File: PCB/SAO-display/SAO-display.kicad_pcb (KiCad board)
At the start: 2 copper layers, 69.3 x 80 mm, 48 parts, among them CON1 SAO v1.69bis badge, J1 Conn_01x02, J2 Conn_01x02, J3 Conn_01x02, J4 Conn_01x02, J5 Conn_01x02, J6 Conn_01x02, M1 AliExpress 3256801443409123 M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, M1 AliExpress 3256806041034057, M1 AliExpress 3256806122258440

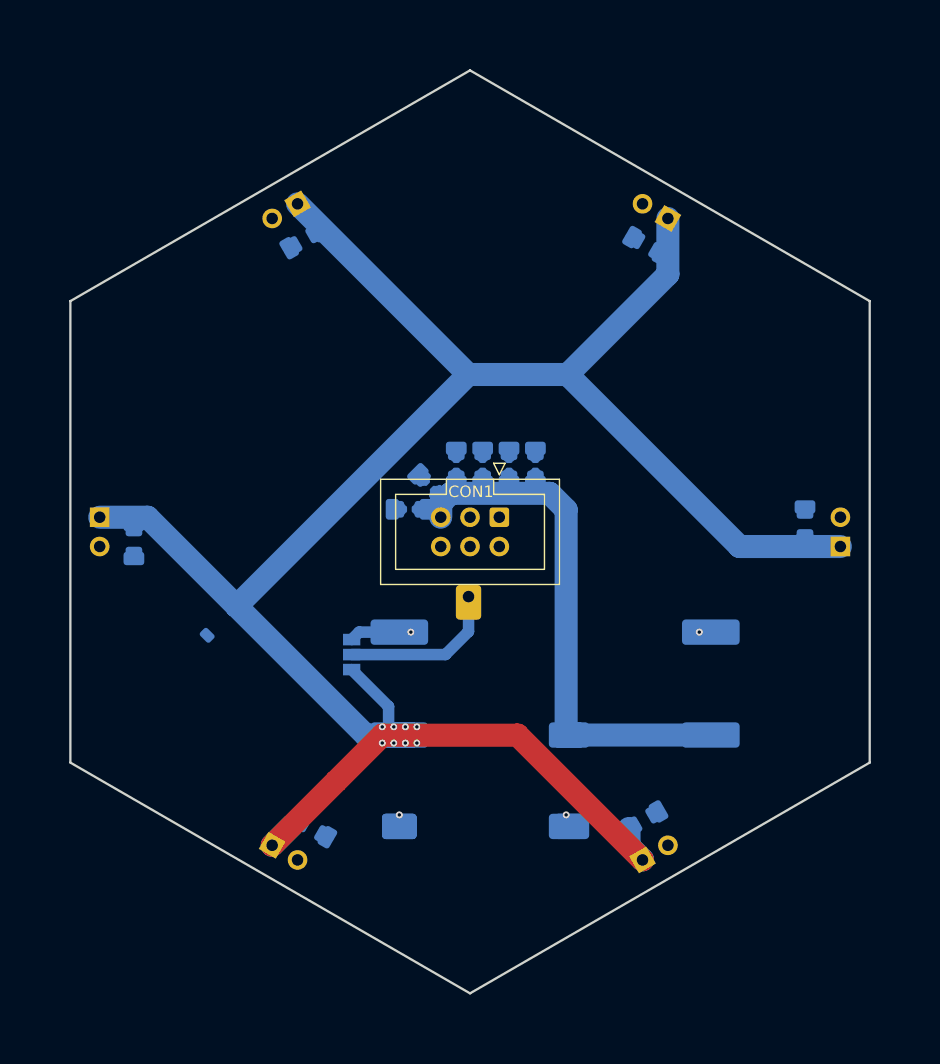
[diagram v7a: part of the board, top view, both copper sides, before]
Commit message: flip connections to half the pogo pins; add protection diode
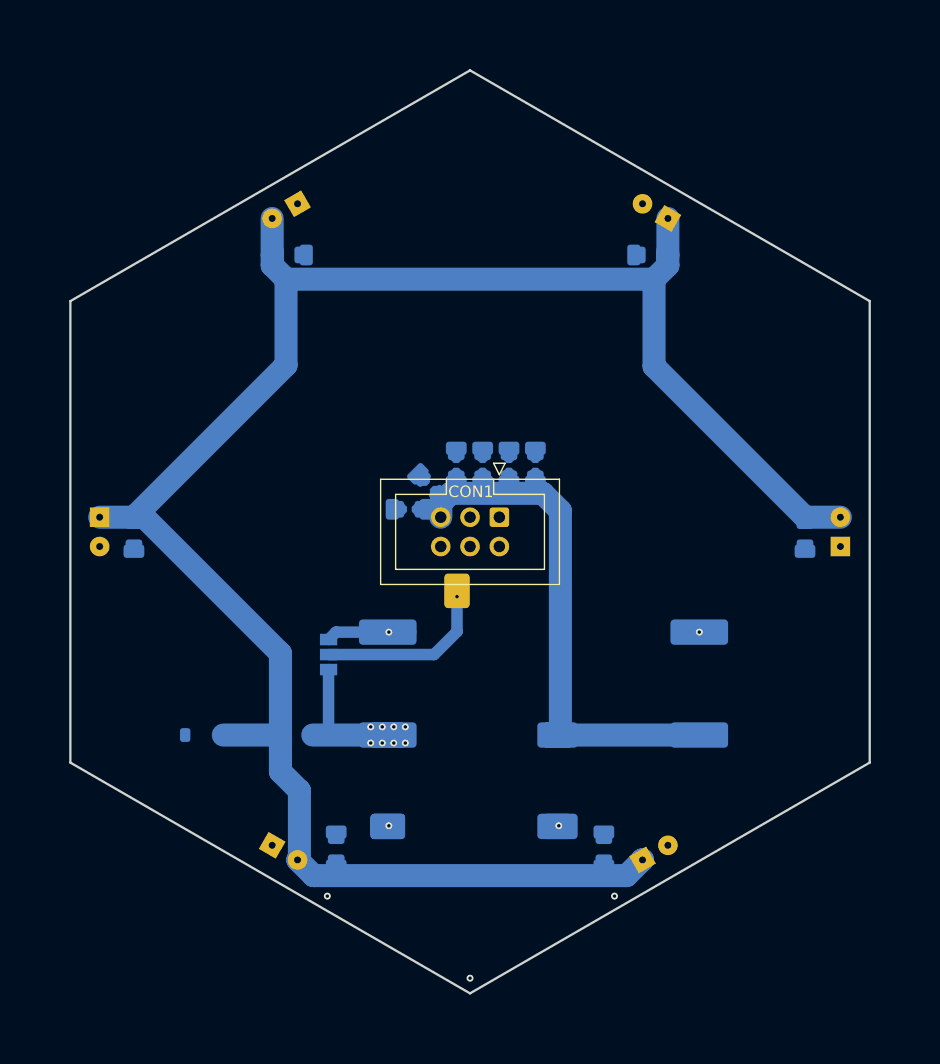
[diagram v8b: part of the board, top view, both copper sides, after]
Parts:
- added Z1: 20V, Diode_SMD:D_SOD-123, B.Cu at (77.0, 117.6)
- C1: value 22+uF 25+V -> 22uF
- C11, C12, C13, C14, C15, C16: value 10+uF -> 10uF
- C2: value 22+uF 50+V -> another 22uF
- C3, C4, C5, C6: value 22+uF 50+V -> 22uF
- D1: value 20V -> 1N5819W S4; footprint Diode_SMD:D_SOD-123 -> Diode_SMD:D_SOD-123F
- J1, J3, J5: value Conn_01x02 -> pogo pins
- J2, J4, J6: value Conn_01x02 -> pads
- M1: value AliExpress 3256806122258440 -> ~
- M1: value AliExpress 3256806041034057 -> ~
- M1: value AliExpress 3256801443409123 Mini560 -> ~
- moved D1 11.8 mm to (85.0, 117.6), turned to 180 degrees
- moved C3 4.29 mm to (111.6, 127.5), turned to 90 degrees
- moved C1_1206 4.29 mm to (111.6, 127.5), turned to 90 degrees
- moved C4 2.71 mm to (88.4, 127.5), turned to 90 degrees
- moved C1_1206 2.70 mm to (88.4, 127.5), turned to 90 degrees
- moved JP1 2.00 mm to (87.7, 110.6)
- moved C1_1206 1.84 mm to (84.3, 76.0), turned to 0 degrees
- moved C6 1.84 mm to (84.3, 76.0), turned to 0 degrees
- moved M1 1.00 mm to (92.9, 117.6) (x2)
- moved M1 1.00 mm to (93.9, 117.6)
- moved C1 0.89 mm to (115.7, 76.0), turned to 180 degrees
- moved C1_1206 0.89 mm to (115.7, 76.0), turned to 180 degrees
- moved C1_1206 0.89 mm to (129.0, 100.2), turned to -90 degrees
- moved C2 0.89 mm to (129.0, 100.2), turned to -90 degrees
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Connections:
- C1 pad 1: Vin -> Vsup
- C1_1206 pad 1: Vin -> Vsup (x6)
- C2 pad 1: Vin -> Vsup
- C3 pad 1: Vin -> Vsup
- C4 pad 1: Vin -> Vsup
- C5 pad 1: Vin -> Vsup
- C6 pad 1: Vin -> Vsup
- D1 pad 2: GND -> Vsup
- J1 pad 1: Vin -> Vsup
- J2 pad 1: Vin -> GND
- J2 pad 2: GND -> Vsup
- J3 pad 1: Vin -> Vsup
- J4 pad 1: Vin -> GND
- J4 pad 2: GND -> Vsup
- J5 pad 1: Vin -> Vsup
- J6 pad 1: Vin -> GND
- J6 pad 2: GND -> Vsup
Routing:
- net Vin: track 191.9 -> 14.6 mm
- net Vsup: track 0.00 -> 173.8 mm
- net GND: track 5.40 -> 7.40 mm, vias 4 -> 7
- net enable: track 14.0 -> 15.0 mm
